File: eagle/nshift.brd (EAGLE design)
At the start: 160 x 100 mm, 15 parts, among them IC1 TINY13V-10PU, IC2 7805T, Q1 IRF510, Q2 IRF510

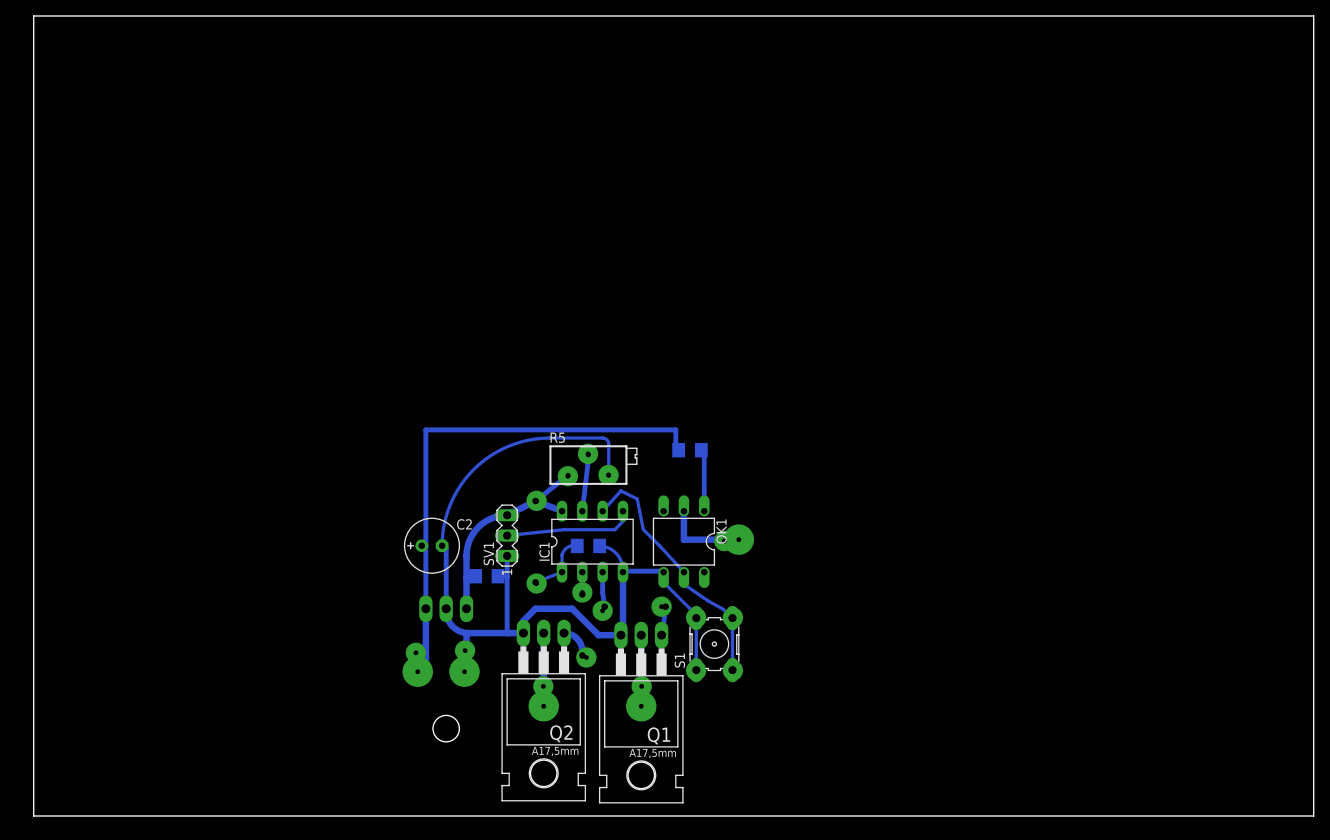
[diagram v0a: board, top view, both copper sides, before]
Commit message: refactor for new soic components
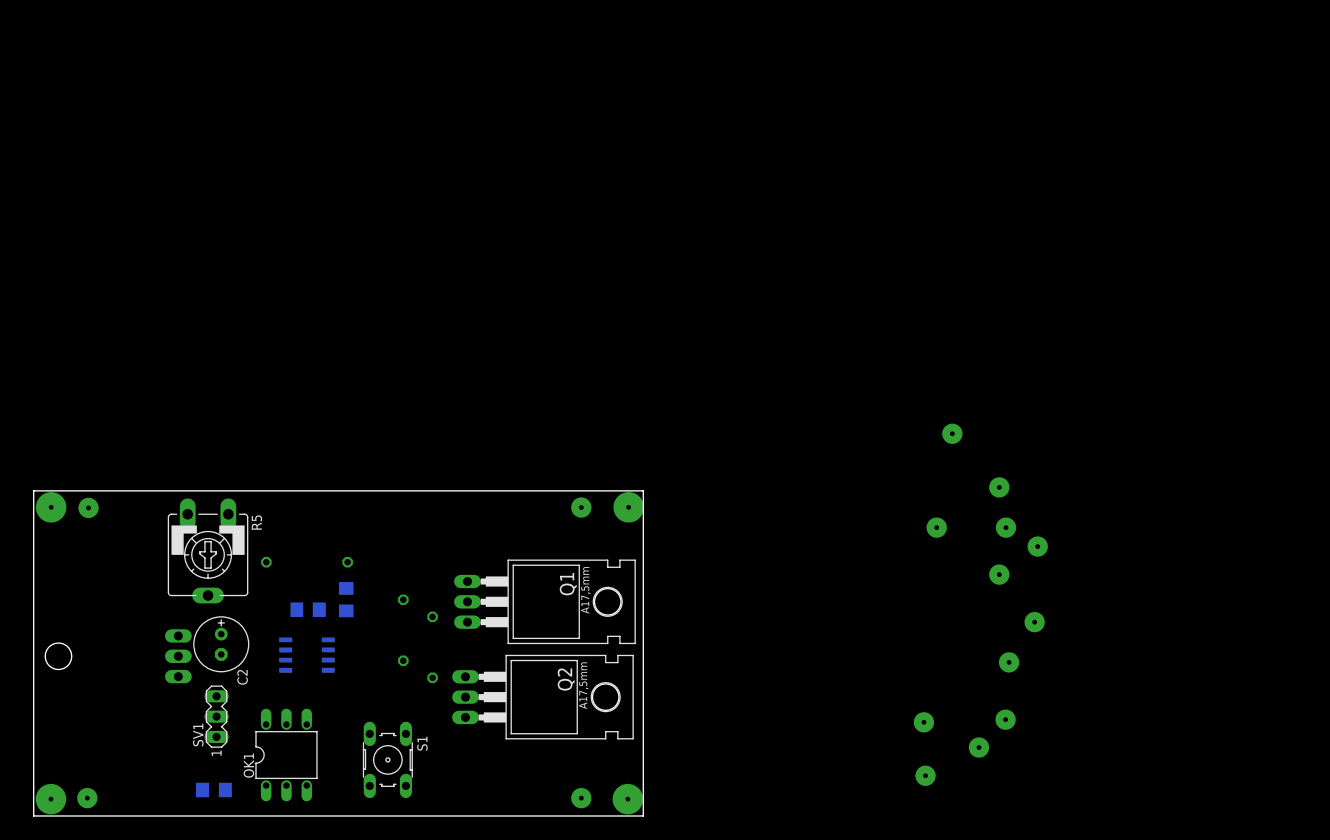
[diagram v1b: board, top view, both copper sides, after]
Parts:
- IC1: value TINY13V-10PU -> TINY13-20SSU; device atmel:DIL08 -> atmel:8S1
- R5: device resistor:RTRIMT93XB -> pot:CA9V
- moved R1 73.1 mm to (22.5, 3.25)
- moved OK1 56.4 mm to (31.6, 7.62), turned to 0 degrees
- moved R5 48.9 mm to (21.8, 32.6), turned to 180 degrees
- moved IC2 43.8 mm to (7.92, 20.0), turned to 270 degrees
- moved S1 43.3 mm to (44.3, 7.01), turned to 270 degrees
- moved SV1 42.8 mm to (22.9, 12.4)
- moved IC1 38.4 mm to (34.2, 20.1), flipped to the bottom, turned to 270 degrees
- moved C1 31.0 mm to (39.1, 27.1), turned to 90 degrees
- moved R3 29.1 mm to (46.2, 23.2), turned to 90 degrees
- moved C2 29.1 mm to (23.4, 21.5), turned to 270 degrees
- moved R2 28.7 mm to (34.2, 31.7), turned to 0 degrees
- moved C3 22.7 mm to (34.3, 25.8)
- moved R4 18.9 mm to (49.9, 21.1)
- moved Q1 18.6 mm to (60.6, 26.8), turned to 270 degrees
- moved Q2 3.81 mm to (60.3, 14.9), turned to 270 degrees
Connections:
- net SELECT renamed MULTIPLY
- net +5V: now also R5.E; no longer R5.1
- net ADC: now also R5.S; no longer R5.2
- net GND: now also R5.A; no longer R5.3
- net N_EN_IN: now also S1.3, S1.4
- net N_EN_OUT: no longer S1.3, S1.4
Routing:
- net GND: track 109.4 -> 0.00 mm, vias 1 -> 0
- net +12V: track 67.3 -> 0.00 mm
- net N_EN_OUT: track 32.4 -> 0.00 mm
- net +5V: track 27.7 -> 0.00 mm
- net MULTIPLY: track 16.2 -> 0.00 mm
- net N$8: track 10.7 -> 0.00 mm, vias 1 -> 0
- net FUEL_R: track 9.65 -> 0.00 mm
- net NITROUS_R: track 9.14 -> 0.00 mm
- net N$1: track 7.98 -> 0.00 mm
- net RESET: track 7.90 -> 0.00 mm
- net ADC: track 7.27 -> 0.00 mm
- net N$9: track 5.33 -> 0.00 mm
- net NITRO_M: track 4.34 -> 0.00 mm
- net N$2: track 3.74 -> 0.00 mm
- net N$3: track 3.60 -> 0.00 mm
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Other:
- board size 160 x 100 mm -> 76.2 x 40.6 mm

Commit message: Готовая плата soic
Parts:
- R2: device resistor:0207/10 -> resistor:R1206
- R3, R4: device resistor:0207/7 -> resistor:R1206
- moved Q1 12.6 mm to (60.1, 14.2)
- moved Q2 11.2 mm to (60.0, 26.0)
- moved R3 4.90 mm to (46.7, 18.3), turned to 180 degrees
- moved R5 4.77 mm to (26.0, 30.5), turned to 270 degrees
- moved C1 4.23 mm to (39.3, 22.8), turned to 180 degrees
- moved R2 4.04 mm to (36.4, 28.4)
- moved C2 3.64 mm to (27.1, 21.2)
- moved IC1 3.63 mm to (37.5, 18.7)
- moved R4 3.51 mm to (46.5, 22.2), turned to 180 degrees
- moved IC2 2.79 mm to (10.7, 20.0)
- moved C3 2.12 mm to (36.4, 25.5)
- moved SV1 1.74 mm to (24.1, 11.2), turned to 135 degrees
- moved S1 1.00 mm to (43.3, 7.11), turned to 0 degrees
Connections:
- net +5V: now also R5.A; no longer R5.E
- net GND: now also R5.E; no longer R5.A
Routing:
- net GND: track 0.00 -> 108.7 mm, vias 0 -> 3
- net N_EN_IN: track 0.00 -> 50.6 mm
- net +5V: track 0.00 -> 49.4 mm
- net +12V: track 0.00 -> 44.1 mm
- net N$6: track 0.00 -> 42.2 mm, vias 1 -> 5
- net ADC: track 0.00 -> 17.9 mm
- net MULTIPLY: track 0.00 -> 13.0 mm
- net N_EN_OUT: track 0.00 -> 11.6 mm
- net N$2: track 0.00 -> 10.8 mm
- net RESET: track 0.00 -> 10.2 mm
- net N$3: track 0.00 -> 6.29 mm
- net N$1: track 0.00 -> 6.13 mm
- net FUEL_M: track 0.00 -> 6.12 mm
- net NITRO_M: track 0.00 -> 5.19 mm
- added copper zone on layer 16, net N$4
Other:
- board outline removed
- board text added: "+12v"
- board text added: "F OUT GND"
- board text added: "GND"
- board text added: "IN GND"
- board text added: "N OUT GND"
- board text added: "NShift2"
